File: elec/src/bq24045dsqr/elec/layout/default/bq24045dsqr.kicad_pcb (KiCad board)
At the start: 2 copper layers, 225.7 x 100.8 mm, 4 parts

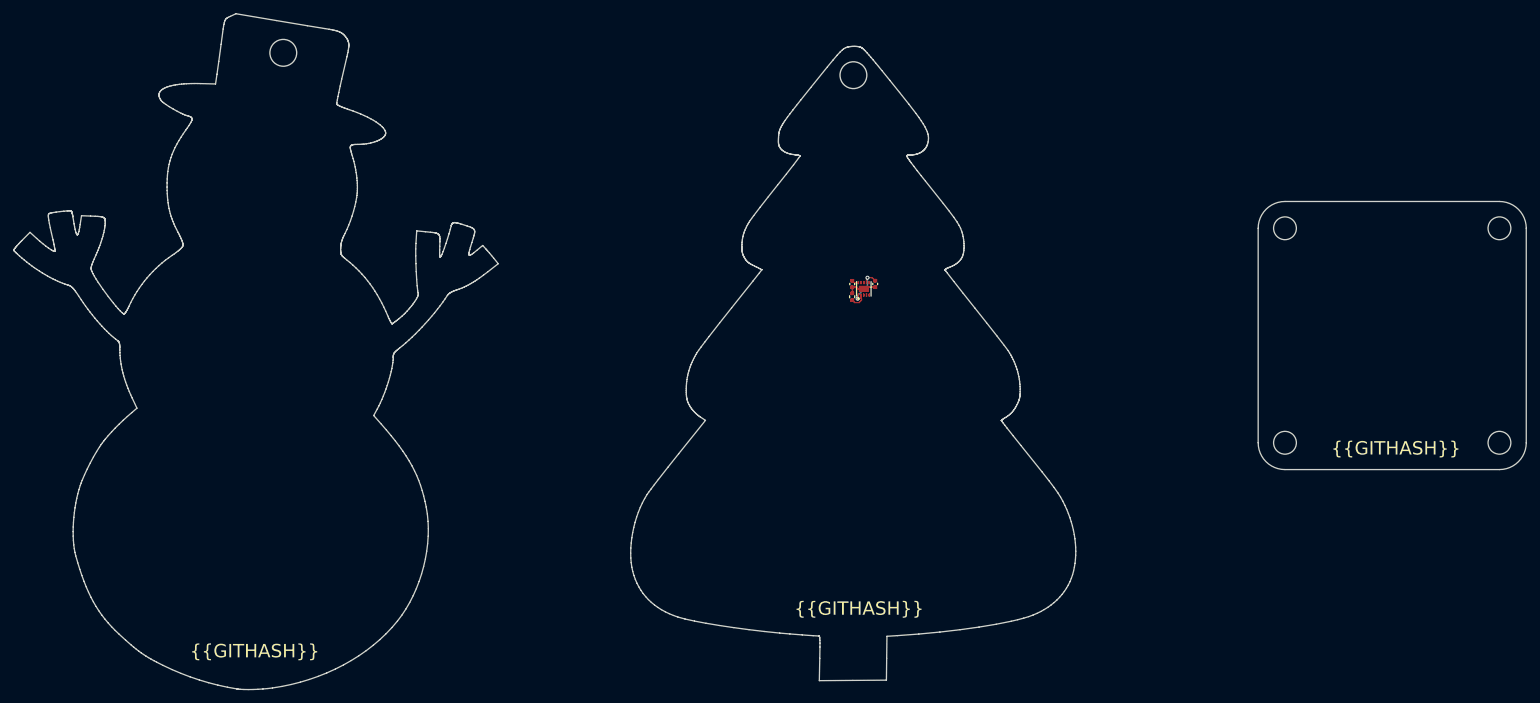
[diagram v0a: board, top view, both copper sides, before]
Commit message: Add layout for base
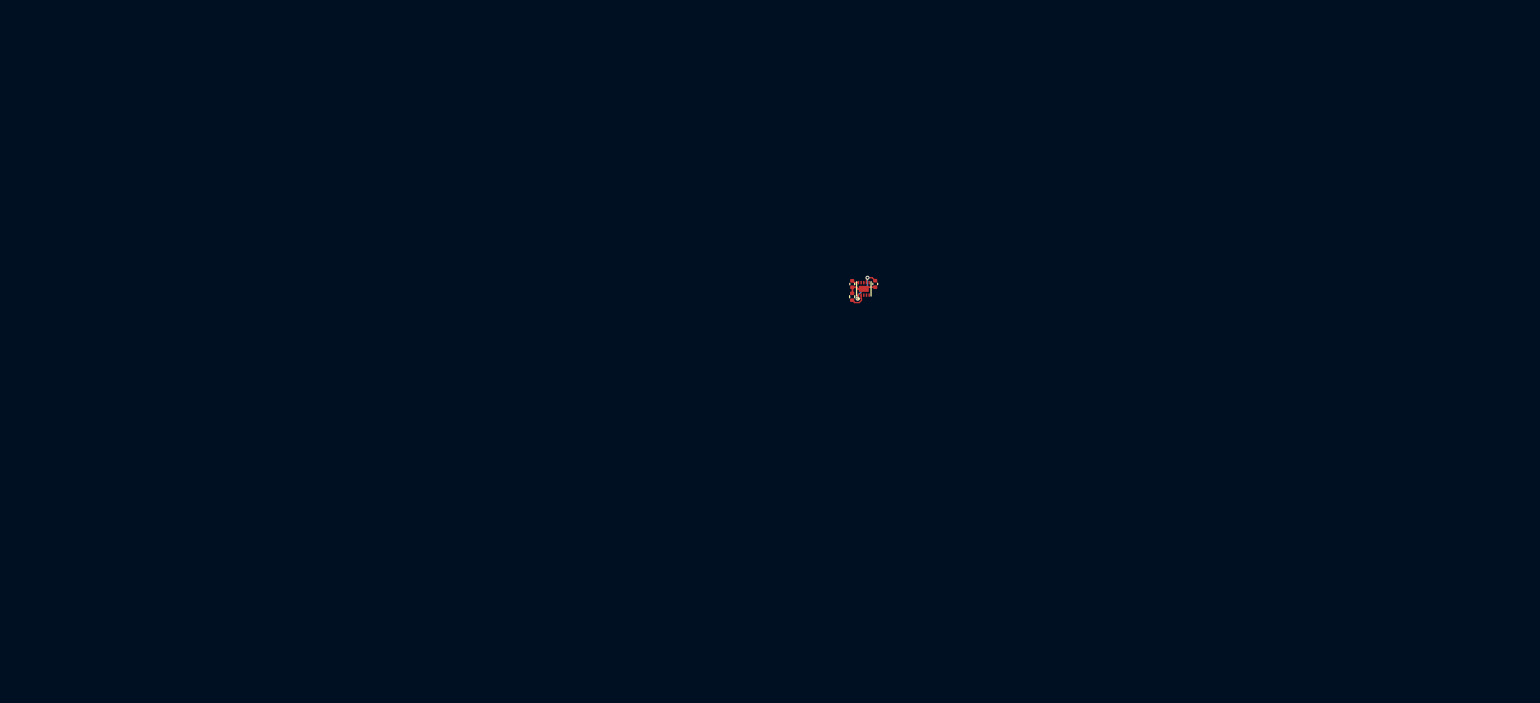
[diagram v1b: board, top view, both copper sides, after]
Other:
- board outline removed
- board text removed: "{{GITHASH}}"
